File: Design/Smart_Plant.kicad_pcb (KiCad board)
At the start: 2 copper layers, 80 x 129.1 mm, 75 parts, among them IC1 TP4056, IC2 TLC555CDR, IC3 AHT20, IC4 RT9080-33GJ5, IC5 ESP32-S2-MINI-1-N4R2, IC6 VEML7700-TR, IC7 MAX17048G+T10, J6 USB-C, Q1 IRLML0100, T1 MMBT2222A, T2 LBSS84LT1G

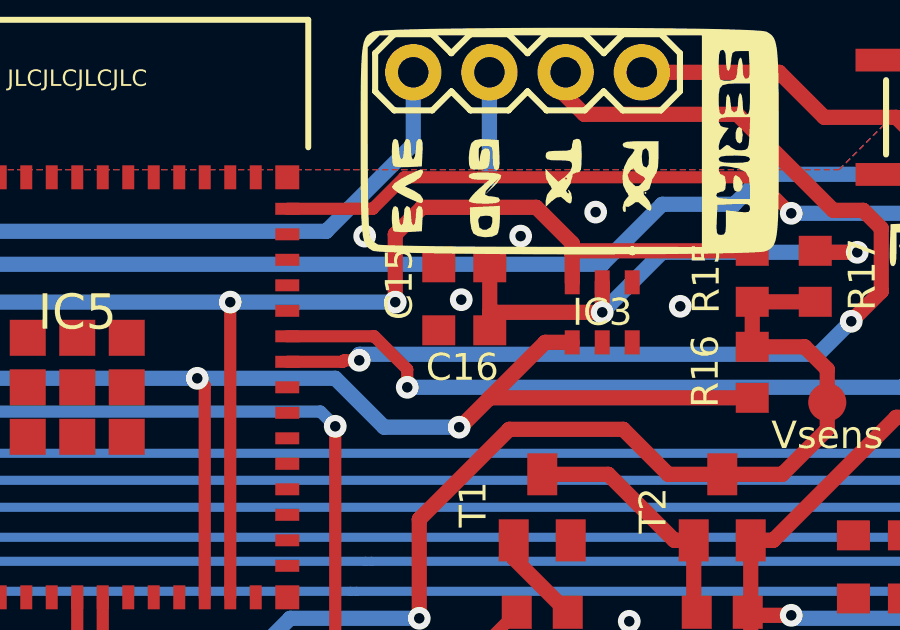
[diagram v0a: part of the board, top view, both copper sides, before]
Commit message: fix(pcb): repair GND issues from the EAGLE to KiCad import
- connect the orphan GND via next to C16 to C16 pad 2 (was an open)
- merge the duplicated F.Cu / B.Cu GND pours into a single two-layer
  "GND" zone, matching V2R2
- use solid zone connection on the SMD GND pads whose thermal relief
  was starved (R18, J1, IC4, C6, IC5, IC2, IC3)

DRC: 0 unconnected items, 0 starved thermals, no new violations.

Co-Authored-By: Claude Opus 5.5 <noreply@anthropic.com>
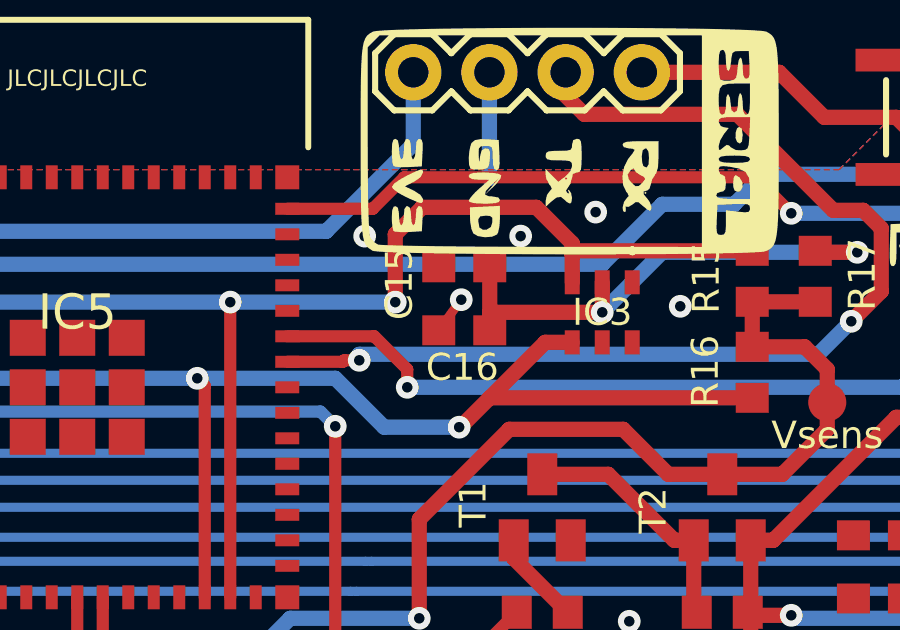
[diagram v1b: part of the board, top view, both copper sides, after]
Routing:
- net GND: track 26.9 -> 28.2 mm
